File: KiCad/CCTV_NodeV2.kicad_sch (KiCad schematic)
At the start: 9 parts, among them J1 Solar 6V/10W, J2 Battery (ext, 2× 18650 ||), U1 CN3791, U2 TC4056A_BMS, U3 MT3608, U4 ESP32-S3-DevKitC-1 N16R8, U5 OV7670

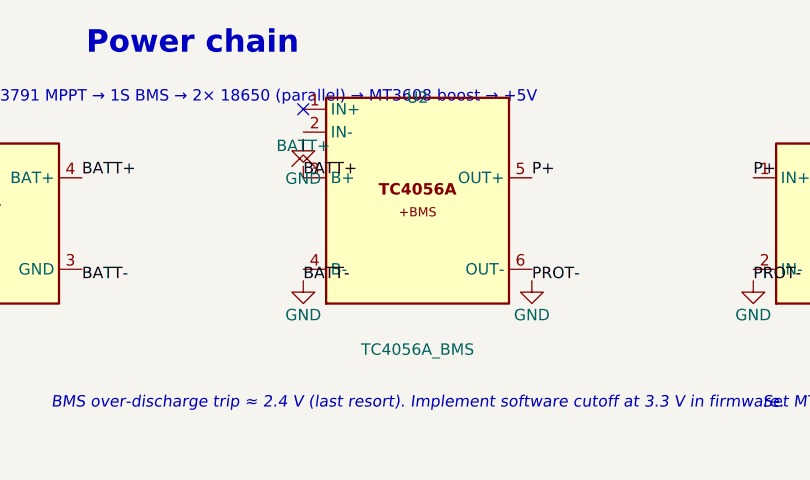
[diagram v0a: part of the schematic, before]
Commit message: Fix TC4056A BMS footprint: 4 pads at BOTTOM EDGE, 4-pin symbol
Physical module (from image): 26x17mm PCB, USB-C charging at top,
4 through-hole solder pads at the BOTTOM EDGE (not in the middle).
Pad order left-to-right: OUT- | B- | B+ | OUT+

TC4056A_BMS_Module.kicad_mod:
- Removed 6 centre pads (IN+/IN- are USB-C handled internally)
- 4 pads repositioned at bottom edge y=+7.5:
    Pad 1 (OUT-/PROT-) : x=-6.75  [square, pin 1 marker]
    Pad 2 (B- /BATT-)  : x=-2.25
    Pad 3 (B+ /BATT+)  : x=+2.25
    Pad 4 (OUT+/P+)    : x=+6.75
- USB-C placeholder at top, IC boxes, LED circles on F.Fab
- Pad spacing ~4.5mm (verify against your specific module)

CCTV_NodeV2.kicad_sch:
- TC4056A_BMS symbol simplified to 4 pins (removed IN+/IN-)
    Pin 1 = B+   → BATT+
    Pin 2 = B-   → BATT-
    Pin 3 = OUT+ → P+
    Pin 4 = OUT- → PROT-
- Removed IN- GND power symbol at (117.3, 60.65)
- Removed IN+ no-connect flag at (117.3, 57.3)

CCTV_NodeV2.kicad_pcb:
- U2 embedded footprint updated with 4-pad bottom-edge geometry
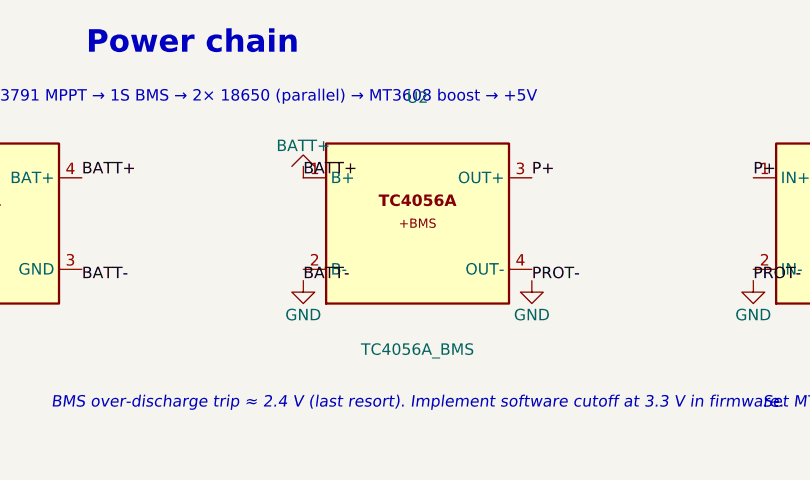
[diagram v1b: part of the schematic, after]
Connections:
- net BATT+: now also U2.1 (B+); no longer U2.3 (B+)
- net BATT-: now also U2.2 (B-); no longer U2.4 (B-)
- net P+: now also U2.3 (OUT+); no longer U2.5 (OUT+)
- net PROT-: now also U2.4 (OUT-); no longer U2.6 (OUT-)
- no-connect marks 1 -> 0
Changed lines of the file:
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@@
 		(pin "3")
 		(pin "4")
-		(pin "5")
-		(pin "6")
 		(instances
 			(project "CCTV_NodeV2"
@@
 	)
 	(symbol
-		(lib_id "CCTV2:GND")
-		(at 117.3 60.65 0)
-		(unit 1)
-		(in_bom yes)
-		(on_board yes)
-		(dnp no)
-		(property "Reference" "#PWR_IN_NEG"
-			(at 117.3 67 0)
-			(hide yes)
-		)
-		(property "Value" "GND"
-			(at 117.3 65 0)
-		)
-		(pin "1")
-		(instances
-			(project "CCTV_NodeV2"
-				(path "/b0c0d0e0-0001-4000-8000-000000000001"
-					(reference "#PWR_IN_NEG")
-					(unit 1)
-				)
-			)
-		)
-	)
-	(no_connect
-		(at 117.3 57.3)
-		(uuid "nc000001-0000-0000-0000-000000000001")
-	)
-	(symbol

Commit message: Redesign TC4056A footprint to match actual module (2+4 pad layout)
Physical layout from image:
  LEFT edge : USB-C connector + 2 pads
                pad 1 = IN+  (top, square)
                pad 2 = IN-  (bottom)
  RIGHT edge: 4 pads at 2.54mm pitch
                pad 3 = OUT+ (top)
                pad 4 = B+
                pad 5 = B-
                pad 6 = OUT- (bottom)
  PCB body: 36mm wide x 22mm tall

TC4056A_BMS_Module.kicad_mod:
- Body: (-18,-11) to (+18,+11) = 36x22mm
- USB-C placeholder on left, IC boxes on centre-right
- Left edge pads: 1(IN+,rect,top) at (-17,-5.5), 2(IN-,circ) at (-17,+5.5)
- Right edge pads: 3(OUT+) at (+17,-3.81), 4(B+) at (+17,-1.27),
                   5(B-) at (+17,+1.27),    6(OUT-) at (+17,+3.81)

CCTV_NodeV2.kicad_sch:
- Symbol restored to 6 pins matching pad numbers:
    Pin 1 (IN+)  on left  → NC (no USB connector yet)
    Pin 2 (IN-)  on left  → GND
    Pin 3 (OUT+) on right → P+     ← BATT+ net preserved
    Pin 4 (B+)   on left  → BATT+  ← P+ net preserved
    Pin 5 (B-)   on left  → BATT-  ← BATT- net preserved
    Pin 6 (OUT-) on right → PROT-  ← PROT- net preserved
- Added GND at IN- position (117.3,60.65)
- Added NC at IN+ position (117.3,57.3)

CCTV_NodeV2.kicad_pcb:
- U2 embedded footprint updated with 6-pad layout
- Net assignments: 1=NC, 2=GND, 3=P+, 4=BATT+, 5=BATT-, 6=PROT-
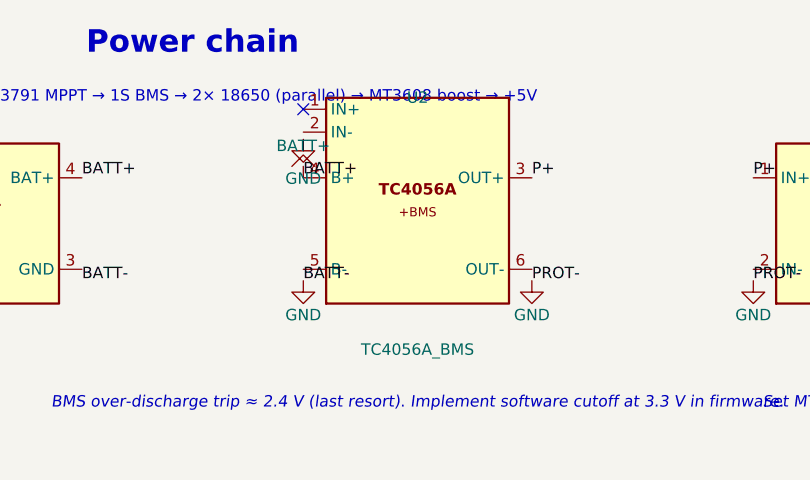
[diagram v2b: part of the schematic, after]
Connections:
- net BATT+: now also U2.4 (B+); no longer U2.1 (B+)
- net BATT-: now also U2.5 (B-); no longer U2.2 (B-)
- net PROT-: now also U2.6 (OUT-); no longer U2.4 (OUT-)
- no-connect marks 0 -> 1
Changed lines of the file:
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@@
 		(pin "3")
 		(pin "4")
+		(pin "5")
+		(pin "6")
 		(instances
 			(project "CCTV_NodeV2"
@@
 	)
 	(symbol
+		(lib_id "CCTV2:GND")
+		(at 117.3 60.65 0)
+		(unit 1)
+		(in_bom yes)
+		(on_board yes)
+		(dnp no)
+		(property "Reference" "#PWR_IN_NEG"
+			(at 117.3 67 0)
+			(hide yes)
+		)
+		(property "Value" "GND"
+			(at 117.3 65 0)
+		)
+		(pin "1")
+		(instances
+			(project "CCTV_NodeV2"
+				(path "/b0c0d0e0-0001-4000-8000-000000000001"
+					(reference "#PWR_IN_NEG")
+					(unit 1)
+				)
+			)
+		)
+	)
+	(no_connect
+		(at 117.3 57.3)
+		(uuid "nc000001-0000-0000-0000-000000000002")
+	)
+	(symbol

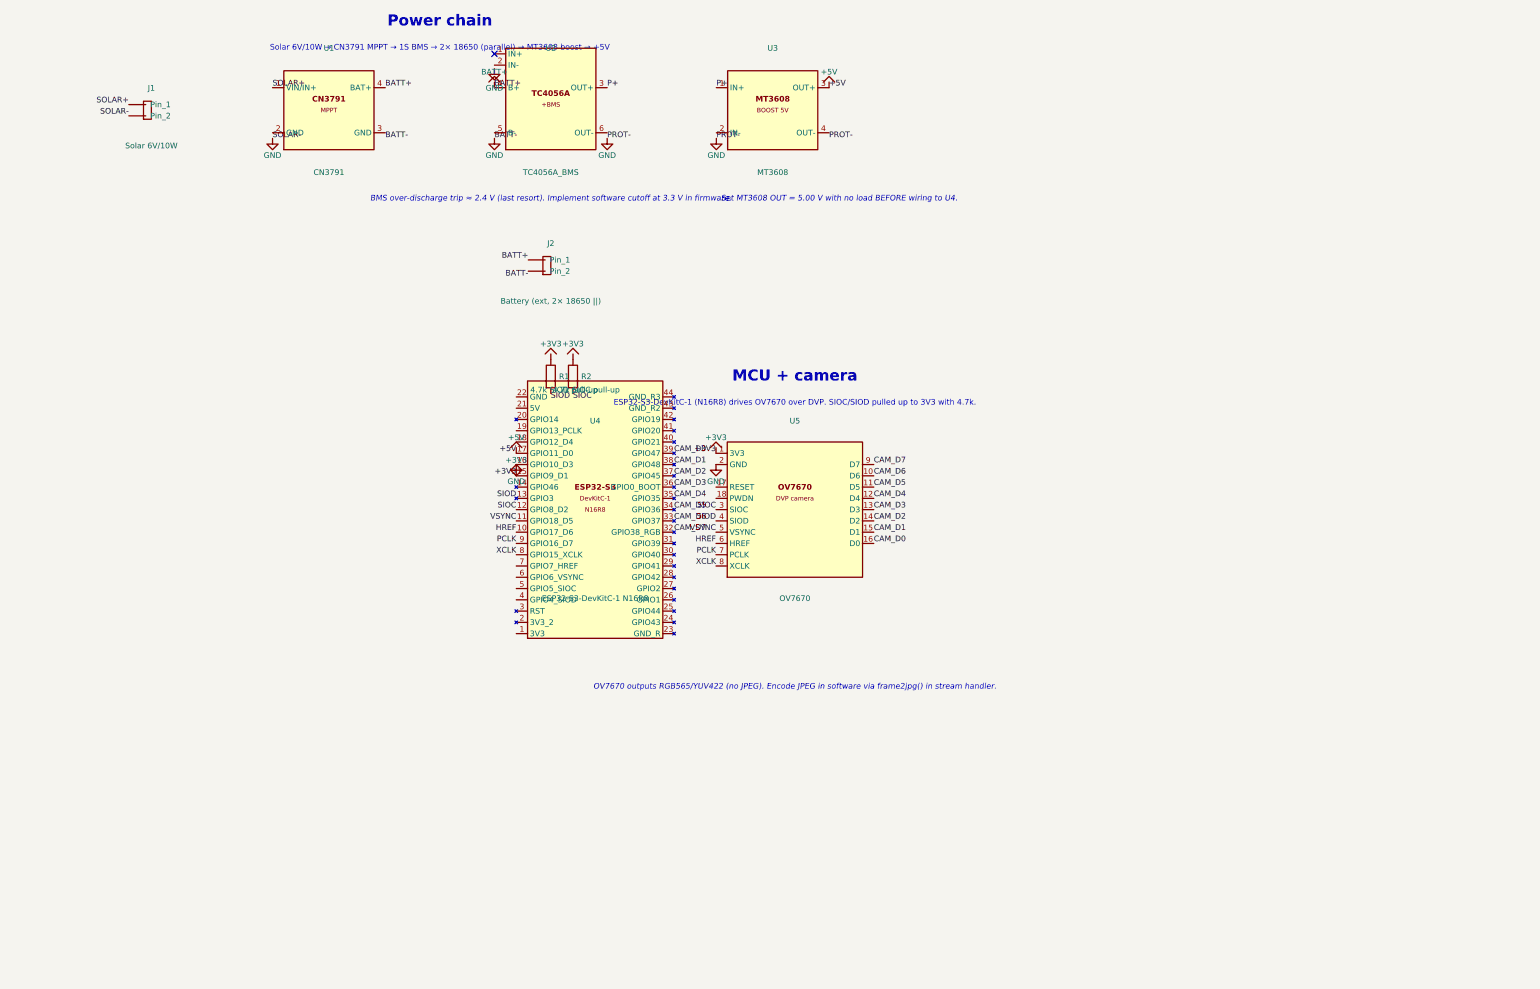
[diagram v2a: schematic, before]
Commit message: Move U4 and U5 apart in schematic for visual clarity
Previous layout had U4 (ESP32-S3, 44-pin, 58mm tall) and U5 (OV7670)
at x=140 and x=185 — only 45mm apart, causing heavy visual overlap.

New positions:
  U4 ESP32-S3-DevKitC-1: (140,160) → (60,220)   [shifted -80x, +60y]
  U5 OV7670:             (185,160) → (290,220)   [shifted +105x, +60y]

Gap between components now ~175mm, giving each symbol its own
clear area. Net labels connect by name within the sheet so all
SIOC, SIOD, VSYNC, HREF, PCLK, XCLK, D0-D7 connections are
preserved without needing physical wire rerouting.

Text annotations repositioned to match:
  'MCU + camera' heading: 185,130 → 175,185
  Description text:       185,136 → 175,191
  OV7670 note:            185,200 → 290,265

Note: pin-adjacent net labels (SIOD, SIOC etc.) still reference
old pin positions — drag them to the new pin stubs in eeschema
after opening.
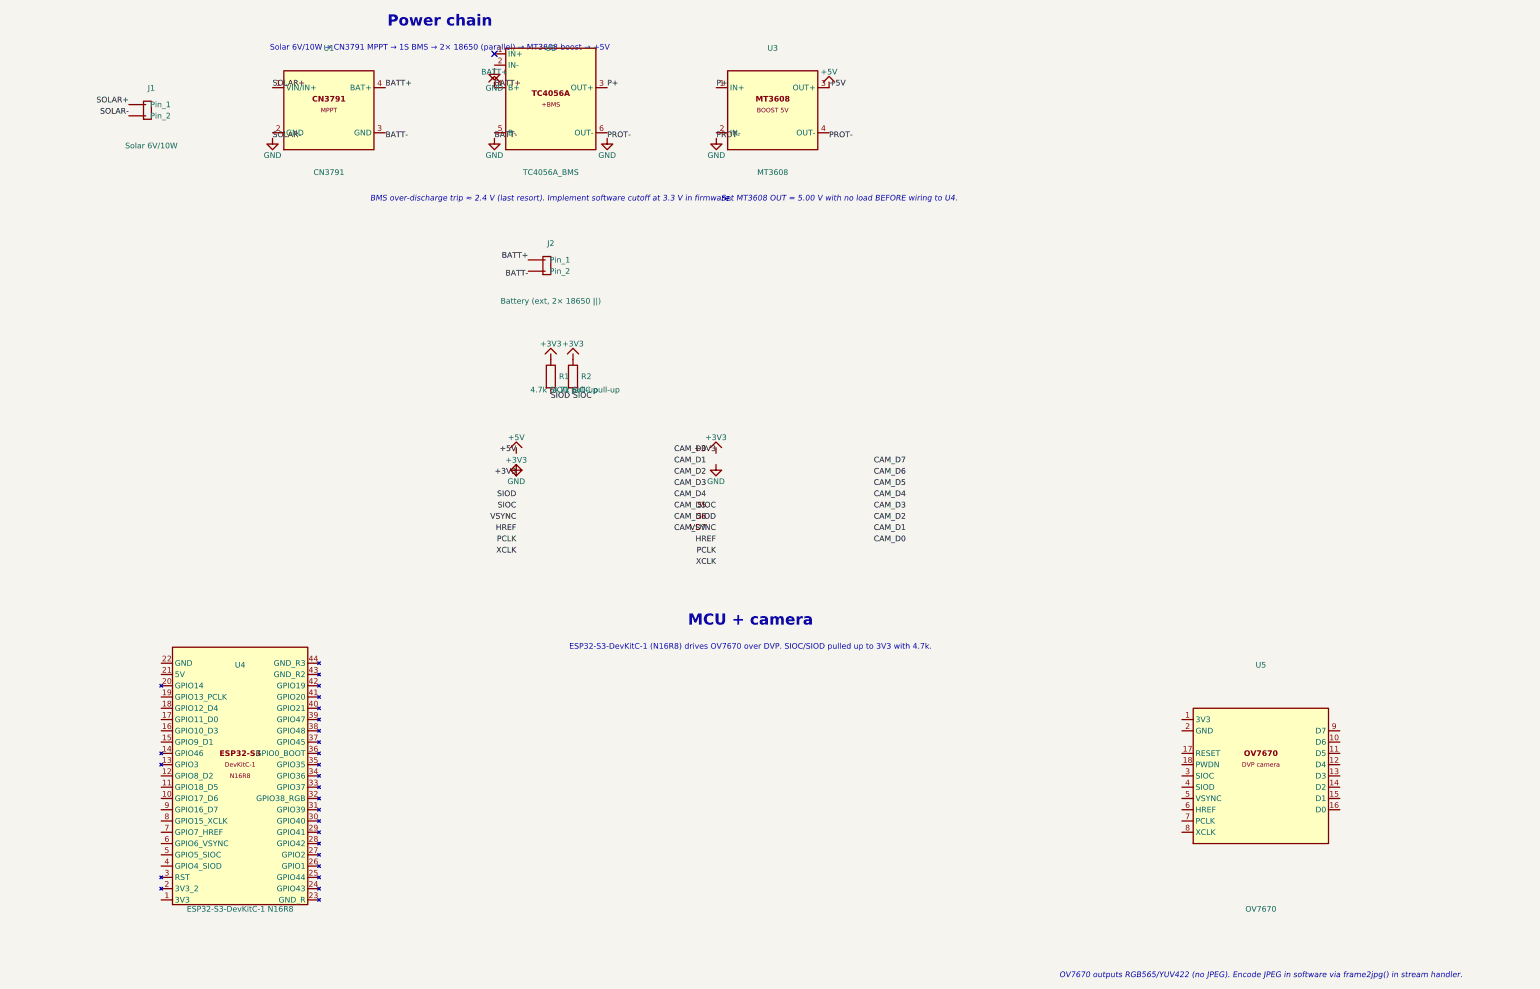
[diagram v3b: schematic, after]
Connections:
- net +3V3: no longer U4.15 (GPIO9_D1), U5.1 (3V3)
- net +5V: no longer U4.17 (GPIO11_D0)
- net CAM_D0: no longer U4.39 (GPIO47), U5.16 (D0)
- net CAM_D1: no longer U4.38 (GPIO48), U5.15 (D1)
- net CAM_D2: no longer U4.37 (GPIO45), U5.14 (D2)
- net CAM_D3: no longer U4.36 (GPIO0_BOOT), U5.13 (D3)
- net CAM_D4: no longer U4.35 (GPIO35), U5.12 (D4)
- net CAM_D5: no longer U4.34 (GPIO36), U5.11 (D5)
- net CAM_D6: no longer U4.33 (GPIO37), U5.10 (D6)
- net CAM_D7: no longer U4.32 (GPIO38_RGB), U5.9 (D7)
- net GND: no longer U4.16 (GPIO10_D3), U5.2 (GND)
- net HREF: no longer U4.10 (GPIO17_D6), U5.6 (HREF)
- net PCLK: no longer U4.9 (GPIO16_D7), U5.7 (PCLK)
- net SIOC: no longer U4.12 (GPIO8_D2), U5.3 (SIOC)
- net SIOD: no longer U4.13 (GPIO3), U5.4 (SIOD)
- net VSYNC: no longer U4.11 (GPIO18_D5), U5.5 (VSYNC)
- net XCLK: no longer U4.8 (GPIO15_XCLK), U5.8 (XCLK)
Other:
- moved on the sheet: U4, U5
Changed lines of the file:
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@@
 	(symbol
 		(lib_id "CCTV2:ESP32_S3_DevKitC")
-		(at 140 160 0)
+		(at 60 220 0)
 		(unit 1)
 		(in_bom yes)
@@
 		(dnp no)
 		(property "Reference" "U4"
-			(at 140 140 0)
+			(at 60 195 0)
 		)
 		(property "Value" "ESP32-S3-DevKitC-1 N16R8"
-			(at 140 180 0)
+			(at 60 250 0)
 		)
 		(property "Footprint" "CCTV_RPi4:ESP32-S3-DevKitC-1"
@@
 	(symbol
 		(lib_id "CCTV2:OV7670")
-		(at 185 160 0)
+		(at 290 220 0)
 		(unit 1)
 		(in_bom yes)
@@
 		(dnp no)
 		(property "Reference" "U5"
-			(at 185 140 0)
+			(at 290 195 0)
 		)
 		(property "Value" "OV7670"
-			(at 185 180 0)
+			(at 290 250 0)
 		)
 		(property "Footprint" "CCTV_RPi4:OV7670_Module"
@@
 	)
 	(text "MCU + camera"
-		(at 185 130 0)
+		(at 175 185 0)
 		(effects (font (size 2.5 2.5) (bold yes)))
 	)
 	(text "ESP32-S3-DevKitC-1 (N16R8) drives OV7670 over DVP. SIOC/SIOD pulled up to 3V3 with 4.7k."
-		(at 185 136 0)
+		(at 175 191 0)
 		(effects (font (size 1.27 1.27)))
 	)
@@
 	)
 	(text "OV7670 outputs RGB565/YUV422 (no JPEG). Encode JPEG in software via frame2jpg() in stream handler."
-		(at 185 200 0)
+		(at 290 265 0)
 		(effects (font (size 1.27 1.27) (italic yes)))
 	)
